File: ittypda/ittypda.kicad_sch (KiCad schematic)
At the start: 147 parts, among them CN1 S2B-PH-SM4-TB, J1 USB_C_Receptacle_USB2.0_14P, SW1 SW_SPDT, U1 STM32F401RETx, U2 BQ24040DSQR, U3 TLV75801PDRV, Y1 16Mhz

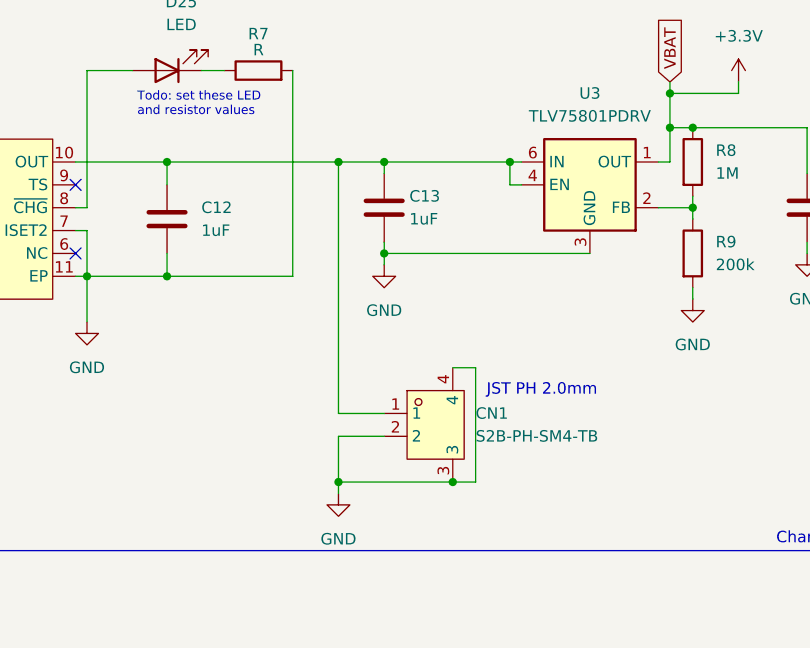
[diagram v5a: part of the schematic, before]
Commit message: fix JST connector side
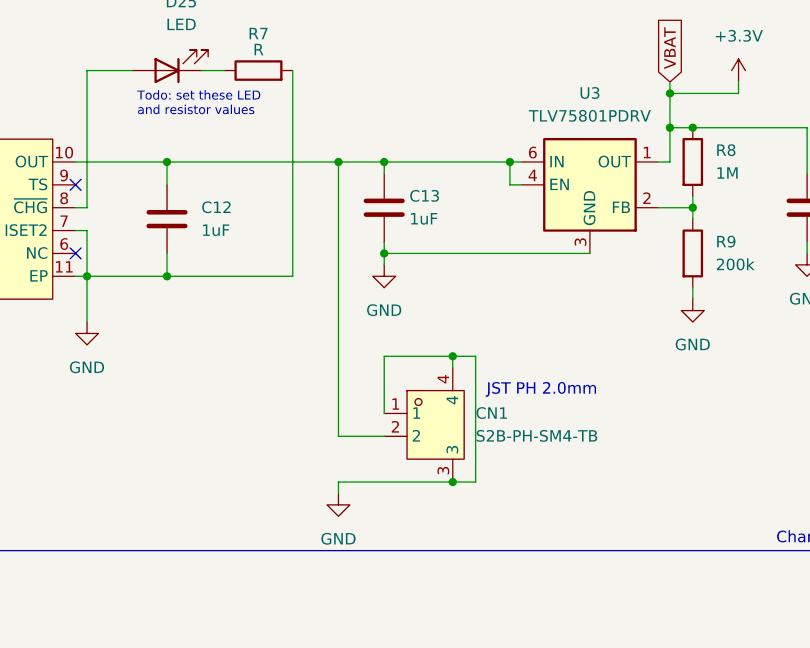
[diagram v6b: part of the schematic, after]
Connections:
- net GND: now also CN1.1; no longer CN1.2
- net at C12.1, C13.1, U2.10 (OUT)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: now also CN1.2; no longer CN1.1
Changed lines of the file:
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@@
 	)
 	(junction
-		(at 172.72 213.36)
-		(diameter 0)
-		(color 0 0 0 0)
-	)
-	(junction
 		(at 90.17 77.47)
 		(diameter 0)
@@
 	)
 	(junction
+		(at 185.42 199.39)
+		(diameter 0)
+		(color 0 0 0 0)
+	)
+	(junction
 		(at 160.02 146.05)
 		(diameter 0)
@@
 	(wire
 		(pts
+			(xy 177.8 199.39) (xy 185.42 199.39)
+		)
+		(stroke
+			(width 0)
+			(type default)
+		)
+	)
+	(wire
+		(pts
 			(xy 132.08 123.19) (xy 146.05 123.19)
 		)
@@
 	(wire
 		(pts
+			(xy 185.42 199.39) (xy 185.42 200.66)
+		)
+		(stroke
+			(width 0)
+			(type default)
+		)
+	)
+	(wire
+		(pts
+			(xy 177.8 208.28) (xy 172.72 208.28)
+		)
+		(stroke
+			(width 0)
+			(type default)
+		)
+	)
+	(wire
+		(pts
 			(xy 106.68 81.28) (xy 106.68 104.14)
 		)
@@
 	(wire
 		(pts
-			(xy 172.72 177.8) (xy 172.72 205.74)
-		)
-		(stroke
-			(width 0)
-			(type default)
-		)
-	)
-	(wire
-		(pts
 			(xy 160.02 100.33) (xy 173.99 100.33)
 		)
@@
 	(wire
 		(pts
-			(xy 172.72 205.74) (xy 177.8 205.74)
-		)
-		(stroke
-			(width 0)
-			(type default)
-		)
-	)
-	(wire
-		(pts
 			(xy 134.62 127) (xy 135.89 127)
 		)
@@
 	(wire
 		(pts
+			(xy 172.72 177.8) (xy 172.72 208.28)
+		)
+		(stroke
+			(width 0)
+			(type default)
+		)
+	)
+	(wire
+		(pts
 			(xy 285.75 163.83) (xy 270.51 163.83)
 		)
@@
 	(wire
 		(pts
-			(xy 187.96 200.66) (xy 187.96 213.36)
+			(xy 187.96 199.39) (xy 187.96 213.36)
 		)
 		(stroke
@@
 	(wire
 		(pts
-			(xy 172.72 208.28) (xy 177.8 208.28)
-		)
-		(stroke
-			(width 0)
-			(type default)
-		)
-	)
-	(wire
-		(pts
 			(xy 148.59 35.56) (xy 148.59 58.42)
 		)
@@
 	(wire
 		(pts
-			(xy 172.72 213.36) (xy 172.72 208.28)
-		)
-		(stroke
-			(width 0)
-			(type default)
-		)
-	)
-	(wire
-		(pts
 			(xy 146.05 100.33) (xy 160.02 100.33)
 		)
@@
 	(wire
 		(pts
-			(xy 185.42 200.66) (xy 187.96 200.66)
+			(xy 185.42 199.39) (xy 187.96 199.39)
 		)
 		(stroke
@@
 		)
 		(stroke
+			(width 0)
+			(type default)
+		)
+	)
+	(wire
+		(pts
+			(xy 177.8 205.74) (xy 177.8 199.39)
+		)
+		(stroke

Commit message: organize schem
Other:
- note added: "FPC Connector"
- note added: "Microcontroller"
- moved on the sheet: C1, C10, C2, C3, C4, C5, C6, C7, C8, C9, D1, D10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

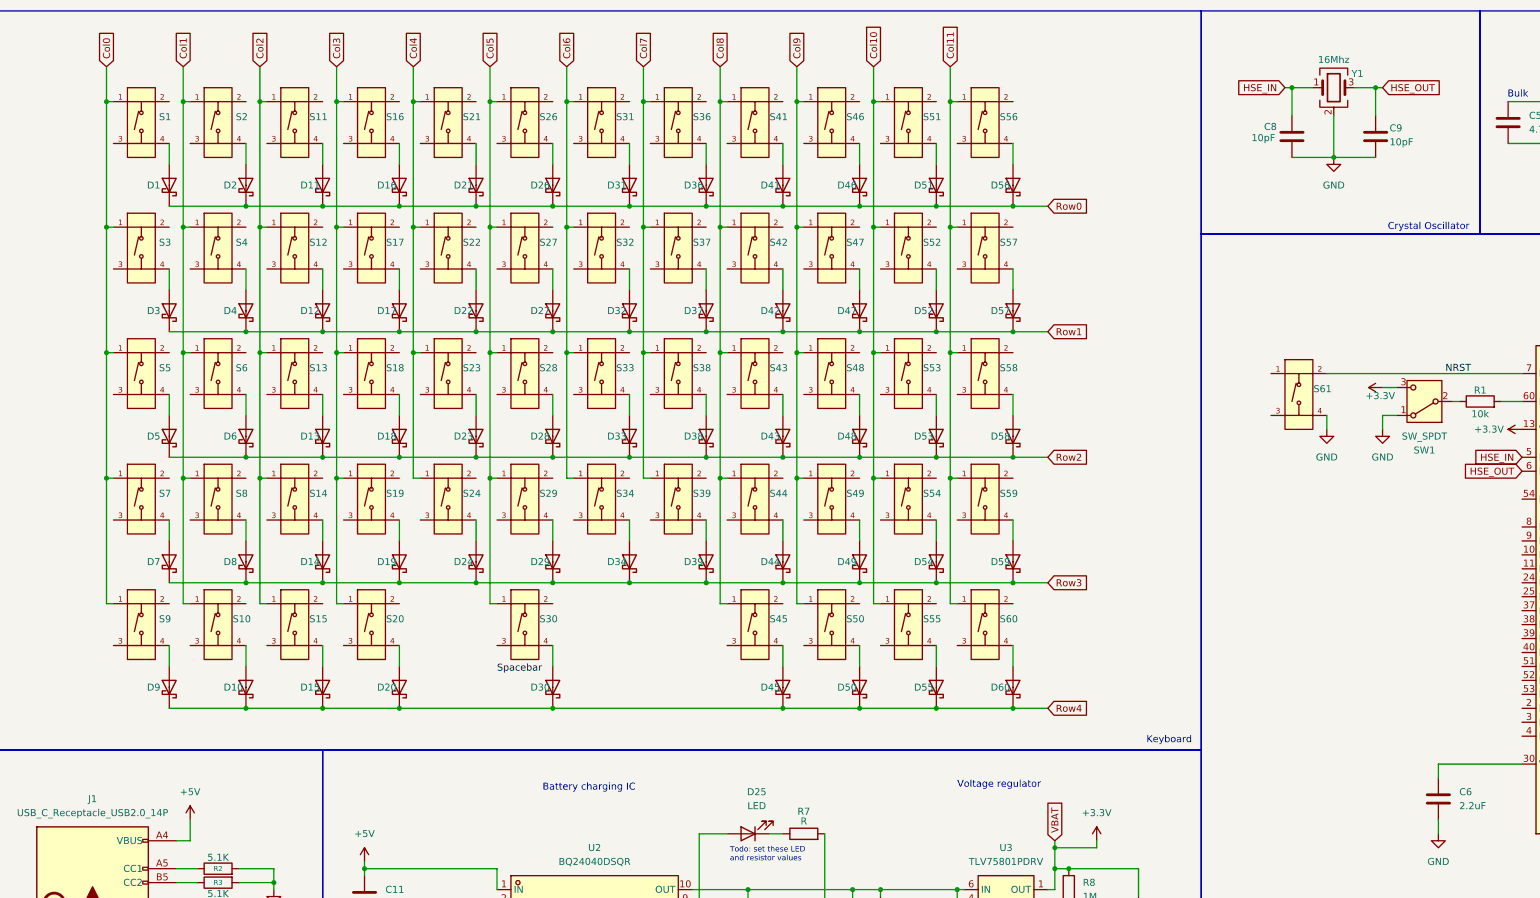
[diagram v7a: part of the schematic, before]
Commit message: replace all old switch symbols
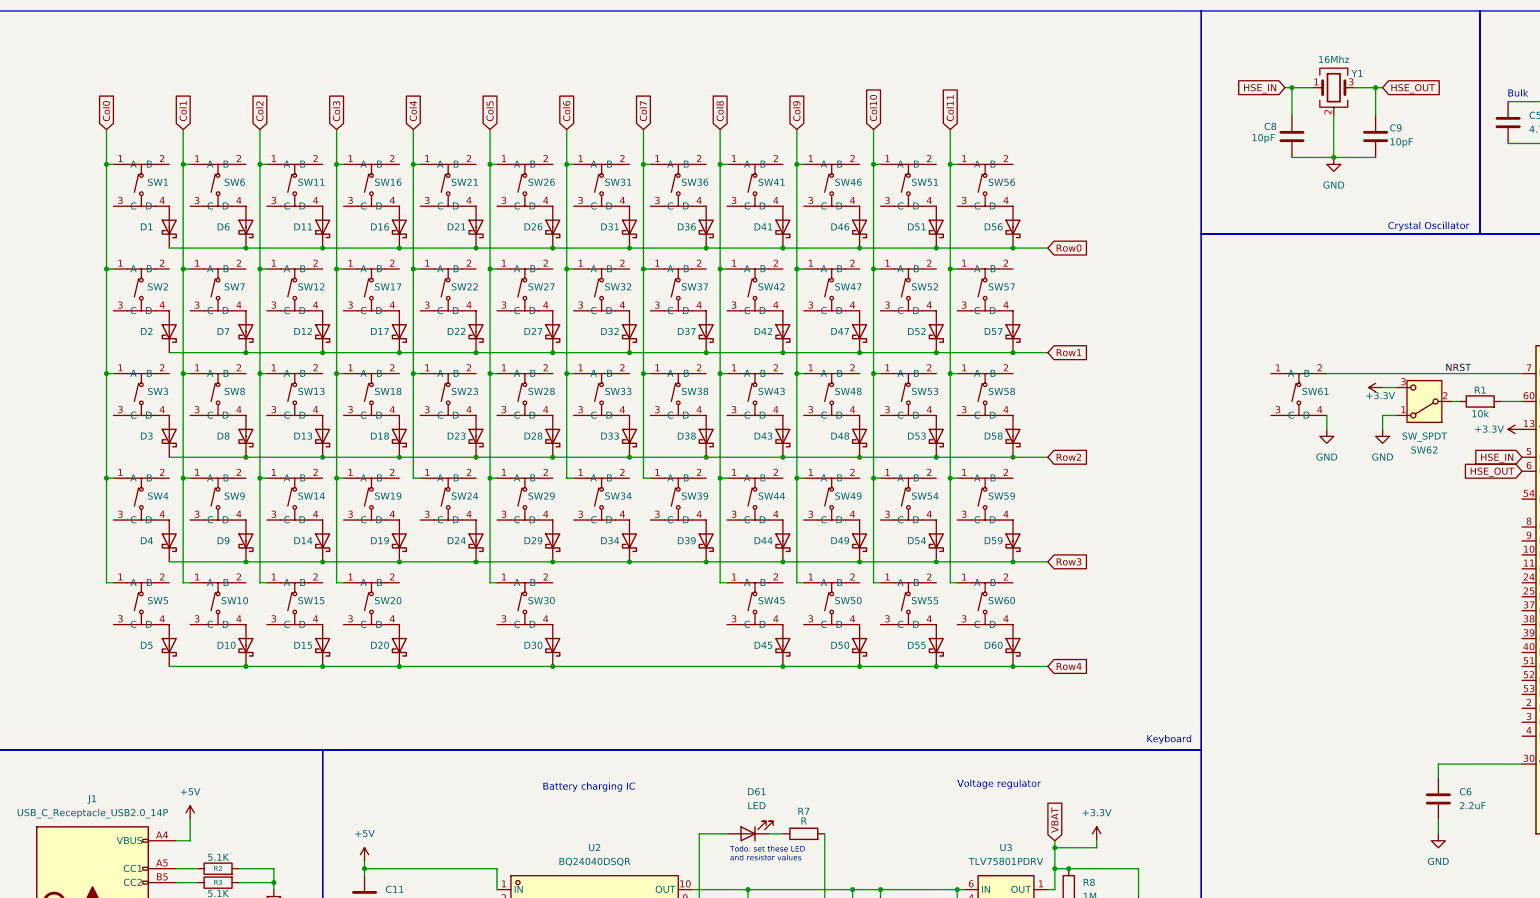
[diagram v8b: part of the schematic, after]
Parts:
- removed S1, S10, S11, S12, S13, S14, S15, S16, S17, S18, S19, S2, S20, S21, S22, S23, S24, S26, S27, S28, S29, S3, S30, S31, S32, S33, S34, S36, S37, S38, S39, S4, S41, S42, S43, S44, S45, S46, S47, S48, S49, S5, S50, S51, S52, S53, S54, S55, S56, S57, S58, S59, S6, S60, S61, S7, S8, S9: Tactile Button, 160gf, easyeda2kicad:SW-SMD_4P-L5.1-W5.1-P3.70-LS6.5-TL_H1.5, symbol PCM_JLCPCB-Connectors_Buttons:Tactile Button, 160gf, 12V, 50mA, 5.1mm
- added SW1, SW10, SW11, SW12, SW13, SW14, SW15, SW16, SW17, SW18, SW19, SW2, SW20, SW21, SW22, SW23, SW24, SW26, SW27, SW28, SW29, SW3, SW30, SW31, SW32, SW33, SW34, SW36, SW37, SW38, SW39, SW4, SW41, SW42, SW43, SW44, SW45, SW46, SW47, SW48, SW49, SW5, SW50, SW51, SW52, SW53, SW54, SW55, SW56, SW57, SW58, SW59, SW6, SW60, SW61, SW7, SW8, SW9: Switch, easyeda2kicad:SW-SMD_4P-L5.1-W5.1-P3.70-LS6.5-TL_H1.5, symbol easyeda2kicad:TS-1187A-B-A-B
- renumbered D25 to D61, SW1 to SW62
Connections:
- net Col0: now also SW1.1 (A), SW2.1 (A), SW3.1 (A), SW4.1 (A), SW5.1 (A)
- net Col1: now also SW10.1 (A), SW6.1 (A), SW7.1 (A), SW8.1 (A), SW9.1 (A)
- net Col10: now also SW51.1 (A), SW52.1 (A), SW53.1 (A), SW54.1 (A), SW55.1 (A)
- net Col11: now also SW56.1 (A), SW57.1 (A), SW58.1 (A), SW59.1 (A), SW60.1 (A)
- net Col2: now also SW11.1 (A), SW12.1 (A), SW13.1 (A), SW14.1 (A), SW15.1 (A)
- net Col3: now also SW16.1 (A), SW17.1 (A), SW18.1 (A), SW19.1 (A), SW20.1 (A)
- net Col4: now also SW21.1 (A), SW22.1 (A), SW23.1 (A), SW24.1 (A)
- net Col5: now also SW26.1 (A), SW27.1 (A), SW28.1 (A), SW29.1 (A), SW30.1 (A)
- net Col6: now also SW31.1 (A), SW32.1 (A), SW33.1 (A), SW34.1 (A)
- net Col7: now also SW36.1 (A), SW37.1 (A), SW38.1 (A), SW39.1 (A)
- net Col8: now also SW41.1 (A), SW42.1 (A), SW43.1 (A), SW44.1 (A), SW45.1 (A)
- net Col9: now also SW46.1 (A), SW47.1 (A), SW48.1 (A), SW49.1 (A), SW50.1 (A)
- net GND: now also SW61.4 (D)
- net NRST: now also SW61.2 (B)
- net Row0: now also D6.1; no longer D2.1
- net Row1: now also D2.1, D7.1; no longer D3.1, D4.1
- net Row2: now also D3.1, D8.1; no longer D5.1, D6.1
- net Row3: now also D4.1, D9.1; no longer D7.1, D8.1
- net Row4: now also D5.1; no longer D9.1
- net at D16.2: now also SW16.4 (D)
- net at D39.2: now also SW39.4 (D)
- net at D28.2: now also SW28.4 (D)
- net at D7.2: now also SW7.4 (D)
- net at D6.2: now also SW6.4 (D)
- net at D23.2: now also SW23.4 (D)
- net at D5.2: now also SW5.4 (D)
- net at D41.2: now also SW41.4 (D)
- net at D26.2: now also SW26.4 (D)
- net at D56.2: now also SW56.4 (D)
- net at D36.2: now also SW36.4 (D)
- net at D13.2: now also SW13.4 (D)
- net at D11.2: now also SW11.4 (D)
- net at D3.2: now also SW3.4 (D)
- net at D17.2: now also SW17.4 (D)
- net at D48.2: now also SW48.4 (D)
- net at D27.2: now also SW27.4 (D)
- net at D34.2: now also SW34.4 (D)
- net at D60.2: now also SW60.4 (D)
- net at D15.2: now also SW15.4 (D)
- net at D46.2: now also SW46.4 (D)
- net at D32.2: now also SW32.4 (D)
- net at D18.2: now also SW18.4 (D)
- net at D52.2: now also SW52.4 (D)
- net at D45.2: now also SW45.4 (D)
- net at D57.2: now also SW57.4 (D)
- net at D9.2: now also SW9.4 (D)
- net at D33.2: now also SW33.4 (D)
- net at D43.2: now also SW43.4 (D)
- net at D51.2: now also SW51.4 (D)
- net at D21.2: now also SW21.4 (D)
- net at D55.2: now also SW55.4 (D)
- net at D4.2: now also SW4.4 (D)
- net at D37.2: now also SW37.4 (D)
- net at D47.2: now also SW47.4 (D)
- net at D14.2: now also SW14.4 (D)
- net at D49.2: now also SW49.4 (D)
- net at D2.2: now also SW2.4 (D)
- net at D10.2: now also SW10.4 (D)
- net at D1.2: now also SW1.4 (D)
- net at D24.2: now also SW24.4 (D)
- net at D59.2: now also SW59.4 (D)
- net at D20.2: now also SW20.4 (D)
- net at D53.2: now also SW53.4 (D)
- net at D29.2: now also SW29.4 (D)
- net at D42.2: now also SW42.4 (D)
- net at D58.2: now also SW58.4 (D)
- net at D19.2: now also SW19.4 (D)
- net at D44.2: now also SW44.4 (D)
- net at D22.2: now also SW22.4 (D)
- net at D31.2: now also SW31.4 (D)
- net at D54.2: now also SW54.4 (D)
- net at D8.2: now also SW8.4 (D)
- net at D50.2: now also SW50.4 (D)
- net at D38.2: now also SW38.4 (D)
- net at D30.2: now also SW30.4 (D)
- net at D12.2: now also SW12.4 (D)
